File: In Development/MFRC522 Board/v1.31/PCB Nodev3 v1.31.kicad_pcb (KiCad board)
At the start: 2 copper layers, 120 x 50 mm, 37 parts, among them P1 ESP32 NODEMCU DEVKIT1 LEFT HE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, P2 ESP32 NODEMCU DEVKIT1 RIGHT H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, Q2 Q_NPN_BEC, U1 MFRC522, Y1 27.12 MHz

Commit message: redrew, and anotatted some caps and leds
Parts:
- added H1: MountingHole, MountingHole:MountingHole_3.2mm_M3, F.Cu at (40.9, 62.7)
- added H2: MountingHole, MountingHole:MountingHole_3.2mm_M3, F.Cu at (40.9, 102.7)
- added H3: MountingHole, MountingHole:MountingHole_3.2mm_M3, F.Cu at (150.9, 62.7)
- added H4: MountingHole, MountingHole:MountingHole_3.2mm_M3, F.Cu at (150.9, 102.7)
- added H5: ToolingHole, Custom:TOOLING_HOLE_JLCPCB_SMT, F.Cu at (40.9, 72.7)
- added H6: ToolingHole, Custom:TOOLING_HOLE_JLCPCB_SMT, F.Cu at (40.9, 92.7)
- added H7: ToolingHole, Custom:TOOLING_HOLE_JLCPCB_SMT, F.Cu at (151.3, 82.7)
- added LG1: Logo_Open_Hardware_Small, Custom:OSHWLOGO_TOP_0.2, F.Cu at (40.9, 82.7)
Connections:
- P1 pad 1: (no net) -> Net-(P1-Pad1)
- P1 pad 12: (no net) -> Net-(P1-Pad12)
- P1 pad 13: (no net) -> Net-(P1-Pad13)
- P1 pad 2: (no net) -> Net-(P1-Pad2)
- P1 pad 3: (no net) -> Net-(P1-Pad3)
- P1 pad 4: (no net) -> Net-(P1-Pad4)
- P1 pad 7: (no net) -> Net-(P1-Pad7)
- P2 pad 1: (no net) -> Net-(P2-Pad1)
- P2 pad 11: (no net) -> Net-(P2-Pad11)
- P2 pad 12: (no net) -> Net-(P2-Pad12)
- P2 pad 13: (no net) -> Net-(P2-Pad13)
- P2 pad 15: (no net) -> Net-(P2-Pad15)
- P2 pad 2: (no net) -> Net-(P2-Pad2)
- P2 pad 4: (no net) -> Net-(P2-Pad4)
- P2 pad 5: (no net) -> Net-(P2-Pad5)
- U1 pad 1: (no net) -> Net-(U1-Pad1)
- U1 pad 19: (no net) -> Net-(U1-Pad19)
- U1 pad 20: (no net) -> Net-(U1-Pad20)
- U1 pad 25: (no net) -> Net-(U1-Pad25)
- U1 pad 26: (no net) -> Net-(U1-Pad26)
- U1 pad 27: (no net) -> Net-(U1-Pad27)
- U1 pad 28: (no net) -> Net-(U1-Pad28)
- U1 pad 7: (no net) -> Net-(U1-Pad7)
- U1 pad 8: (no net) -> Net-(U1-Pad8)
- U1 pad 9: (no net) -> Net-(U1-Pad9)
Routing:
- net GND: track 852.4 -> 851.8 mm
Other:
- net class JLCPCB added: clearance 0.127, trace_width 0.254, via_dia 0.8, via_drill 0.4
- board text added: "v1.31"
- board text removed: "v1.3"

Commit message: Added logo.
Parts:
- P1, P2: moved to B.Cu
- turned P1 to 270 degrees
- turned P2 to 270 degrees
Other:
- board text added: "Antenna design and matching circuit adapted from the Adafruit PN532 Breakout Innexgo LLC"
- board text removed: "Adafruit PN532 Breakout"
- board text removed: "Antenna design and matching"
- board text removed: "Designed by Probably an Asian"
- board text removed: "For the NodeMCU"
- board text removed: "Innexgo LLC"
- board text removed: "circuit adapted from the"

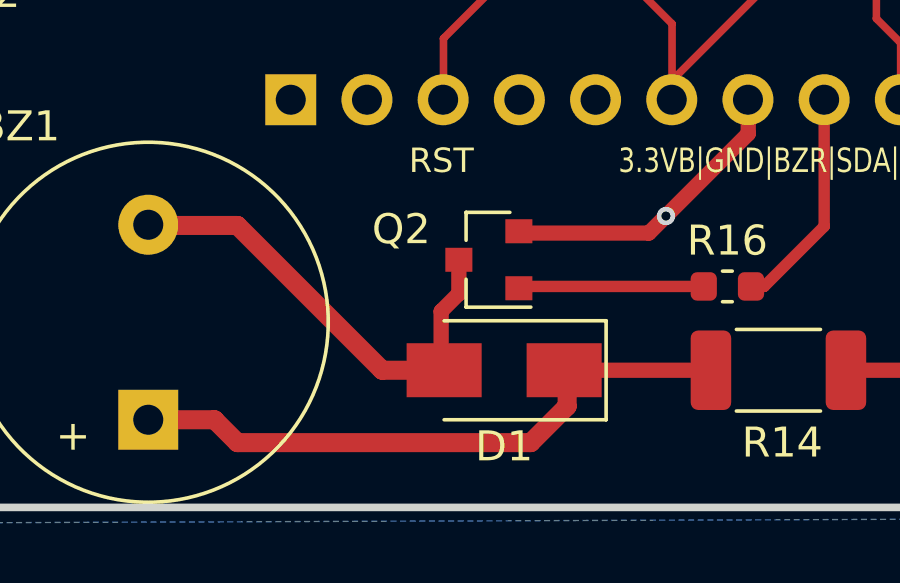
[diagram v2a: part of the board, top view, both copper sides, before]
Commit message: moved a trace
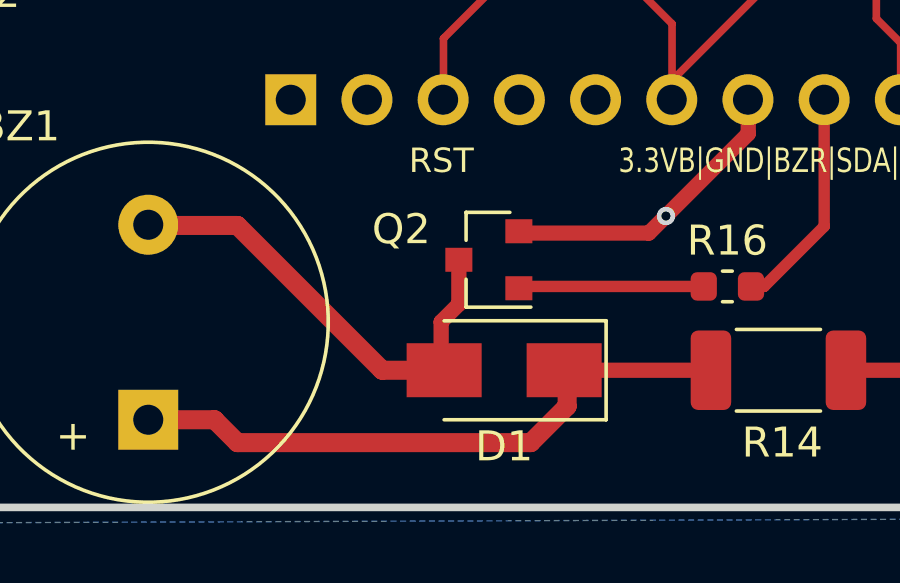
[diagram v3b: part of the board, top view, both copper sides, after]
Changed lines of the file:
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@@
   (segment (start 123.997 100.33) (end 123.936 100.391) (width 0.381) (layer F.Cu) (net 26))
   (segment (start 130.0987 100.33) (end 123.997 100.33) (width 0.381) (layer F.Cu) (net 26))
-  (segment (start 121.936 100.568) (end 121.936 99.441) (width 0.508) (layer F.Cu) (net 27))
-  (segment (start 121.344 103.124) (end 121.344 101.16) (width 0.508) (layer F.Cu) (net 27))
-  (segment (start 121.344 101.16) (end 121.936 100.568) (width 0.508) (layer F.Cu) (net 27))
   (segment (start 114.554 98.298) (end 111.6064 98.298) (width 0.635) (layer F.Cu) (net 27))
   (segment (start 111.6064 98.298) (end 111.5822 98.2738) (width 0.635) (layer F.Cu) (net 27))
   (segment (start 121.444 103.124) (end 119.38 103.124) (width 0.635) (layer F.Cu) (net 27))
   (segment (start 119.38 103.124) (end 114.554 98.298) (width 0.635) (layer F.Cu) (net 27))
+  (segment (start 121.936 100.920997) (end 121.936 99.441) (width 0.508) (layer F.Cu) (net 27))
+  (segment (start 121.344 103.124) (end 121.344 101.512997) (width 0.508) (layer F.Cu) (net 27))
+  (segment (start 121.344 101.512997) (end 121.936 100.920997) (width 0.508) (layer F.Cu) (net 27))
   (segment (start 125.544 103.124) (end 130.088 103.124) (width 0.508) (layer F.Cu) (net 28))
   (segment (start 125.545 102.614) (end 125.544 102.615) (width 0.508) (layer F.Cu) (net 28))

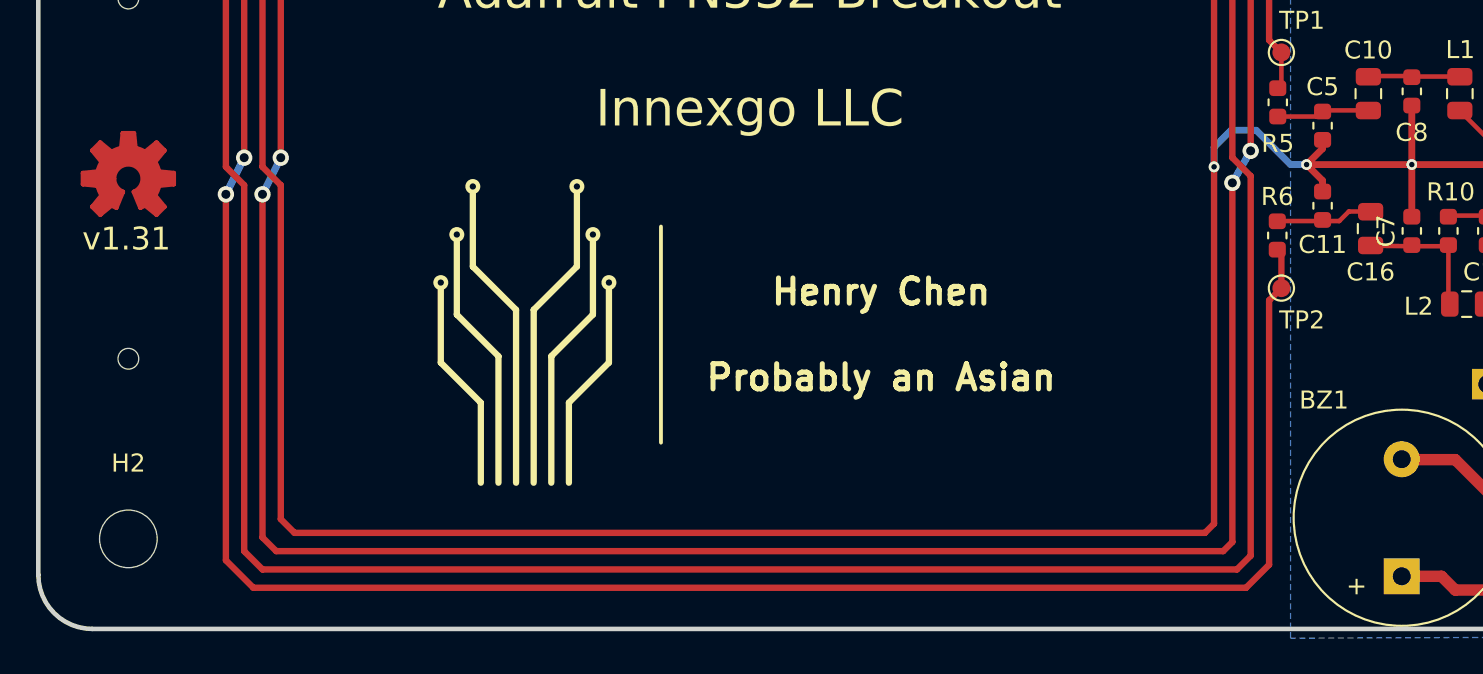
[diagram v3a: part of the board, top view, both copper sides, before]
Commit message: Moved Logo, changed some 3dmodels.
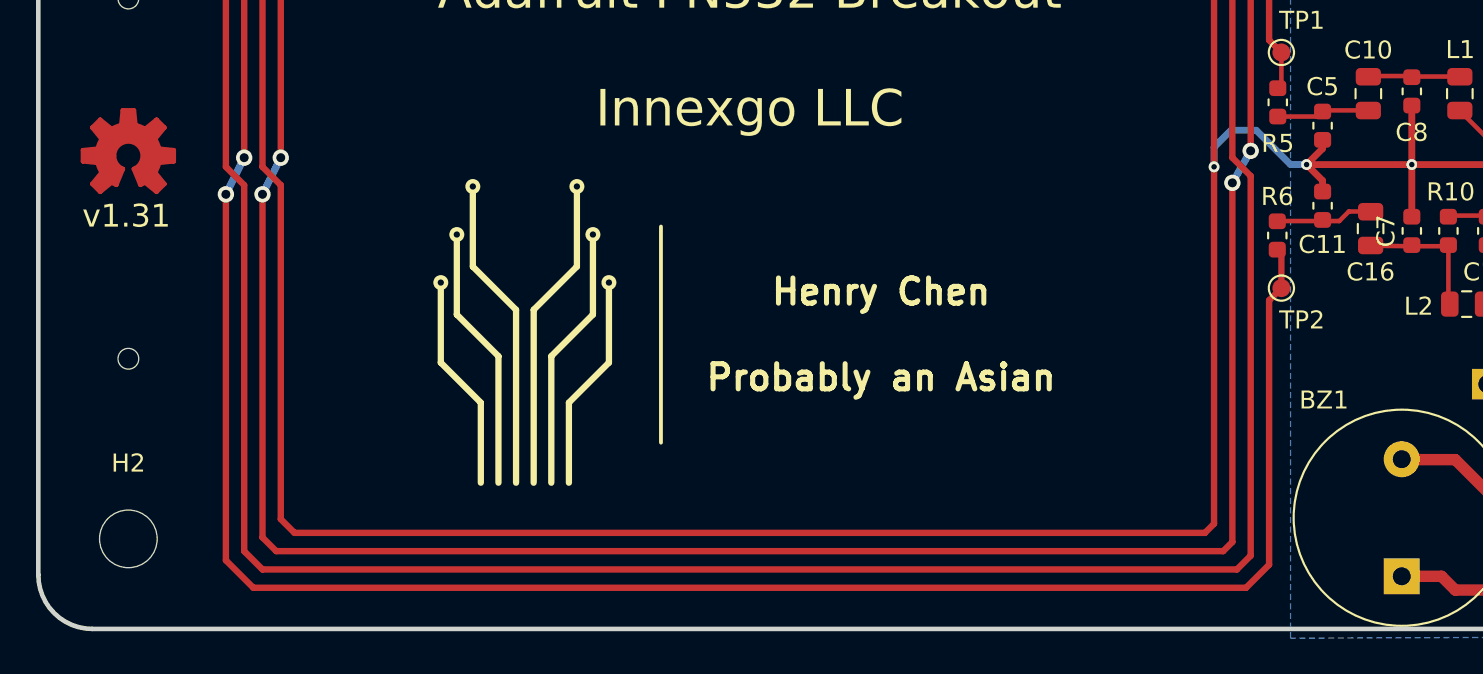
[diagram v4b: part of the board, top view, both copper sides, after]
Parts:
- moved LG1 1.27 mm to (40.9, 81.4)
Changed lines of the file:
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@@
     (add_net "Net-(Q2-Pad1)")
+  )
+  (module Oscillator:Oscillator_SMD_EuroQuartz_XO32-4Pin_3.2x2.5mm (layer F.Cu)
+    (at 142.875 84.201 90)
+    (descr "Miniature Crystal Clock Oscillator EuroQuartz XO32 series, http://cdn-reichelt.de/documents/datenblatt/B400/XO32.pdf, 3.2x2.5mm^2 package")
+    (tags "SMD SMT crystal oscillator")
+    (attr smd)
+    (fp_text reference Y1 (at 0.889 2.667 180) (layer F.SilkS)
+      (effects (font (size 1 1) (thickness 0.15)))
+    )
+    (fp_text value "27.12 MHz" (at 0 2.45 90) (layer F.Fab)
+      (effects (font (size 1 1) (thickness 0.15)))
+    )
+    (fp_circle (center 0 0) (end 0.058333 0) (layer F.Adhes) (width 0.116667))
+    (fp_circle (center 0 0) (end 0.133333 0) (layer F.Adhes) (width 0.083333))
+    (fp_circle (center 0 0) (end 0.208333 0) (layer F.Adhes) (width 0.083333))
+    (fp_circle (center 0 0) (end 0.25 0) (layer F.Adhes) (width 0.1))
+    (fp_line (start 1.9 -1.5) (end -1.9 -1.5) (layer F.CrtYd) (width 0.05))
+    (fp_line (start 1.9 1.5) (end 1.9 -1.5) (layer F.CrtYd) (width 0.05))
+    (fp_line (start -1.9 1.5) (end 1.9 1.5) (layer F.CrtYd) (width 0.05))
+    (fp_line (start -1.9 -1.5) (end -1.9 1.5) (layer F.CrtYd) (width 0.05))
+    (fp_line (start -1.6 0.25) (end -0.6 1.25) (layer F.Fab) (width 0.1))
+    (fp_line (start -1.6 -1.15) (end -1.5 -1.25) (layer F.Fab) (width 0.1))
+    (fp_line (start -1.6 1.15) (end -1.6 -1.15) (layer F.Fab) (width 0.1))
+    (fp_line (start -1.5 1.25) (end -1.6 1.15) (layer F.Fab) (width 0.1))
+    (fp_line (start 1.5 1.25) (end -1.5 1.25) (layer F.Fab) (width 0.1))
+    (fp_line (start 1.6 1.15) (end 1.5 1.25) (layer F.Fab) (width 0.1))
+    (fp_line (start 1.6 -1.15) (end 1.6 1.15) (layer F.Fab) (width 0.1))
+    (fp_line (start 1.5 -1.25) (end 1.6 -1.15) (layer F.Fab) (width 0.1))
+    (fp_line (start -1.5 -1.25) (end 1.5 -1.25) (layer F.Fab) (width 0.1))
+    (fp_text user %R (at 0 0 90) (layer F.Fab)
+      (effects (font (size 0.7 0.7) (thickness 0.105)))
+    )
+    (pad 4 smd rect (at -1.075 -0.775 90) (size 1 0.9) (layers F.Cu F.Paste F.Mask)
+      (net 1 GND))
+    (pad 3 smd rect (at 1.075 -0.775 90) (size 1 0.9) (layers F.Cu F.Paste F.Mask)
+      (net 3 "Net-(C1-Pad2)"))
+    (pad 2 smd rect (at 1.075 0.775 90) (size 1 0.9) (layers F.Cu F.Paste F.Mask)
+      (net 1 GND))
+    (pad 1 smd rect (at -1.075 0.775 90) (size 1 0.9) (layers F.Cu F.Paste F.Mask)
+      (net 4 "Net-(C2-Pad2)"))
+    (model ${KISYS3DMOD}/Custom.3dshapes/Oscillator_SMD_EuroQuartz_XO32-4Pin_3.2x2.5mm.wrl
+      (offset (xyz -1.62 -1.27 0.03))
+      (scale (xyz 0.4 0.4 0.4))
+      (rotate (xyz 0 0 0))
+    )
+  )
+  (module Buzzer_Beeper:Buzzer_12x9.5RM6.5 (layer F.Cu)
+    (at 111.5822 101.5238 90)
+    (descr "Generic Buzzer, D12mm height 9.5mm with RM7.6mm")
+    (tags buzzer)
+    (fp_text reference BZ1 (at 6.5266 -4.318 180) (layer F.SilkS)
+      (effects (font (size 1 1) (thickness 0.15)))
+    )
+    (fp_text value Buzzer (at -0.01 7.4 90) (layer F.Fab)
+      (effects (font (size 1 1) (thickness 0.15)))
+    )
+    (fp_circle (center 0 0) (end 6 0) (layer F.SilkS) (width 0.12))
+    (fp_circle (center -0.01 0) (end 0.99 0) (layer F.Fab) (width 0.1))
+    (fp_circle (center -0.01 0) (end 5.99 0) (layer F.Fab) (width 0.1))
+    (fp_circle (center -0.01 0) (end 6.24 0) (layer F.CrtYd) (width 0.05))
+    (fp_text user %R (at -0.01 -4 90) (layer F.Fab)
+      (effects (font (size 1 1) (thickness 0.15)))
+    )
+    (fp_text user + (at -3.82 -2.54 90) (layer F.Fab)
+      (effects (font (size 1 1) (thickness 0.15)))
+    )
+    (fp_text user + (at -3.82 -2.54 90) (layer F.Fab)
+      (effects (font (size 1 1) (thickness 0.15)))
+    )
+    (pad 2 thru_hole circle (at 3.25 0 90) (size 2 2) (drill 1) (layers *.Cu *.Mask)
+      (net 27 "Net-(BZ1-Pad2)"))
+    (pad 1 thru_hole rect (at -3.25 0 90) (size 2 2) (drill 1) (layers *.Cu *.Mask)
+      (net 28 "Net-(BZ1-Pad1)"))
+    (model ${KISYS3DMOD}/Custom.3dshapes/Buzzer_12x6.5RM6.5.wrl
+      (offset (xyz 0 0 7))
+      (scale (xyz 0.4 0.4 0.4))
+      (rotate (xyz 180 0 0))
+    )
   )
   (module Connector_PinHeader_2.54mm:PinHeader_1x15_P2.54mm_Vertical (layer B.Cu)
@@
   )
   (module Custom:OSHWLOGO_TOP_0.2 (layer F.Cu)
-    (at 40.885 82.696)
+    (at 40.885 81.426)
     (fp_text reference LG1 (at 0 -3.575) (layer F.SilkS) hide
       (effects (font (size 1.143 1.143) (thickness 0.152)) (justify left))
@@
     (pad 1 np_thru_hole circle (at 0 0) (size 3.2 3.2) (drill 3.2) (layers *.Cu *.Mask))
   )
-  (module Buzzer_Beeper:Buzzer_12x9.5RM6.5 (layer F.Cu)
-    (at 111.5822 101.5238 90)
-    (descr "Generic Buzzer, D12mm height 9.5mm with RM7.6mm")
-    (tags buzzer)
-    (fp_text reference BZ1 (at 6.5266 -4.318 180) (layer F.SilkS)
-      (effects (font (size 1 1) (thickness 0.15)))
-    )
-    (fp_text value Buzzer (at -0.01 7.4 90) (layer F.Fab)
-      (effects (font (size 1 1) (thickness 0.15)))
-    )
-    (fp_circle (center 0 0) (end 6 0) (layer F.SilkS) (width 0.12))
-    (fp_circle (center -0.01 0) (end 0.99 0) (layer F.Fab) (width 0.1))
-    (fp_circle (center -0.01 0) (end 5.99 0) (layer F.Fab) (width 0.1))
-    (fp_circle (center -0.01 0) (end 6.24 0) (layer F.CrtYd) (width 0.05))
-    (fp_text user %R (at -0.01 -4 90) (layer F.Fab)
-      (effects (font (size 1 1) (thickness 0.15)))
-    )
-    (fp_text user + (at -3.82 -2.54 90) (layer F.SilkS)
-      (effects (font (size 1 1) (thickness 0.15)))
-    )
-    (fp_text user + (at -3.82 -2.54 90) (layer F.Fab)
-      (effects (font (size 1 1) (thickness 0.15)))
-    )
-    (pad 2 thru_hole circle (at 3.25 0 90) (size 2 2) (drill 1) (layers *.Cu *.Mask)
-      (net 27 "Net-(BZ1-Pad2)"))
-    (pad 1 thru_hole rect (at -3.25 0 90) (size 2 2) (drill 1) (layers *.Cu *.Mask)
-      (net 28 "Net-(BZ1-Pad1)"))
-    (model ${KISYS3DMOD}/Buzzer_Beeper.3dshapes/Buzzer_12x9.5RM7.6.wrl
-      (at (xyz 0 0 0))
-      (scale (xyz 1 1 1))
-      (rotate (xyz 0 0 0))
-    )
-  )
   (module Capacitor_SMD:C_0805_2012Metric (layer F.Cu)
     (at 109.855 85.471 270)
@@
     (pad 1 smd circle (at 0 0) (size 1 1) (layers F.Cu F.Mask)
       (net 1 GND))
-  )
-  (module Oscillator:Oscillator_SMD_EuroQuartz_XO32-4Pin_3.2x2.5mm (layer F.Cu)
-    (at 142.875 84.201 90)
-    (descr "Miniature Crystal Clock Oscillator EuroQuartz XO32 series, http://cdn-reichelt.de/documents/datenblatt/B400/XO32.pdf, 3.2x2.5mm^2 package")
-    (tags "SMD SMT crystal oscillator")
-    (attr smd)
-    (fp_text reference Y1 (at 0.889 2.667 180) (layer F.SilkS)
-      (effects (font (size 1 1) (thickness 0.15)))
-    )
-    (fp_text value "27.12 MHz" (at 0 2.45 90) (layer F.Fab)
-      (effects (font (size 1 1) (thickness 0.15)))
-    )
-    (fp_circle (center 0 0) (end 0.058333 0) (layer F.Adhes) (width 0.116667))
-    (fp_circle (center 0 0) (end 0.133333 0) (layer F.Adhes) (width 0.083333))
-    (fp_circle (center 0 0) (end 0.208333 0) (layer F.Adhes) (width 0.083333))
-    (fp_circle (center 0 0) (end 0.25 0) (layer F.Adhes) (width 0.1))
-    (fp_line (start 1.9 -1.5) (end -1.9 -1.5) (layer F.CrtYd) (width 0.05))
-    (fp_line (start 1.9 1.5) (end 1.9 -1.5) (layer F.CrtYd) (width 0.05))
-    (fp_line (start -1.9 1.5) (end 1.9 1.5) (layer F.CrtYd) (width 0.05))
-    (fp_line (start -1.9 -1.5) (end -1.9 1.5) (layer F.CrtYd) (width 0.05))
-    (fp_line (start -1.6 0.25) (end -0.6 1.25) (layer F.Fab) (width 0.1))
-    (fp_line (start -1.6 -1.15) (end -1.5 -1.25) (layer F.Fab) (width 0.1))
-    (fp_line (start -1.6 1.15) (end -1.6 -1.15) (layer F.Fab) (width 0.1))
-    (fp_line (start -1.5 1.25) (end -1.6 1.15) (layer F.Fab) (width 0.1))
-    (fp_line (start 1.5 1.25) (end -1.5 1.25) (layer F.Fab) (width 0.1))
-    (fp_line (start 1.6 1.15) (end 1.5 1.25) (layer F.Fab) (width 0.1))
-    (fp_line (start 1.6 -1.15) (end 1.6 1.15) (layer F.Fab) (width 0.1))
-    (fp_line (start 1.5 -1.25) (end 1.6 -1.15) (layer F.Fab) (width 0.1))
-    (fp_line (start -1.5 -1.25) (end 1.5 -1.25) (layer F.Fab) (width 0.1))
-    (fp_text user %R (at 0 0 90) (layer F.Fab)
-      (effects (font (size 0.7 0.7) (thickness 0.105)))
-    )
-    (pad 4 smd rect (at -1.075 -0.775 90) (size 1 0.9) (layers F.Cu F.Paste F.Mask)
-      (net 1 GND))
-    (pad 3 smd rect (at 1.075 -0.775 90) (size 1 0.9) (layers F.Cu F.Paste F.Mask)
-      (net 3 "Net-(C1-Pad2)"))
-    (pad 2 smd rect (at 1.075 0.775 90) (size 1 0.9) (layers F.Cu F.Paste F.Mask)
-      (net 1 GND))
-    (pad 1 smd rect (at -1.075 0.775 90) (size 1 0.9) (layers F.Cu F.Paste F.Mask)
-      (net 4 "Net-(C2-Pad2)"))
-    (model ${KISYS3DMOD}/Oscillator.3dshapes/Oscillator_SMD_EuroQuartz_XO32-4Pin_3.2x2.5mm.wrl
-      (at (xyz 0 0 0))
-      (scale (xyz 1 1 1))
-      (rotate (xyz 0 0 0))
-    )
   )
   (module Package_DFN_QFN:QFN-32-1EP_5x5mm_P0.5mm_EP3.1x3.1mm (layer F.Cu)
@@
     (effects (font (size 2.032 2.032) (thickness 0.203)))
   )
-  (gr_text "v1.31\n" (at 40.7797 86.0425) (layer F.SilkS)
+  (gr_text "v1.31\n" (at 40.7797 84.7725) (layer F.SilkS)
     (effects (font (size 1.27 1.27) (thickness 0.152)))
   )
